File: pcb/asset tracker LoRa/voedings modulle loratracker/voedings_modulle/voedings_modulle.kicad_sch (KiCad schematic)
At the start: 3 parts

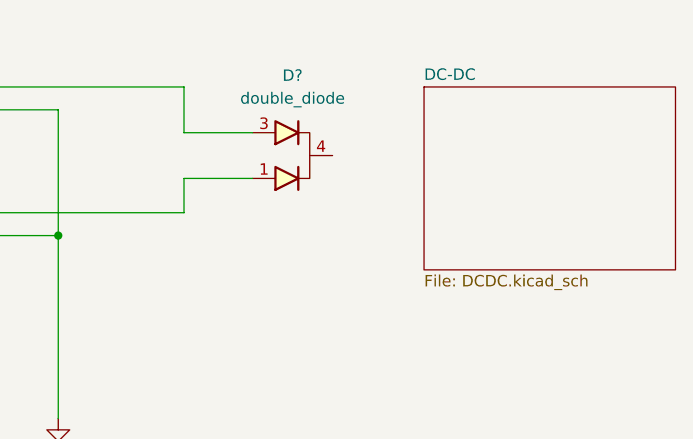
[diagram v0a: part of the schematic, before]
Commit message: ref design
esp32prog refrence design
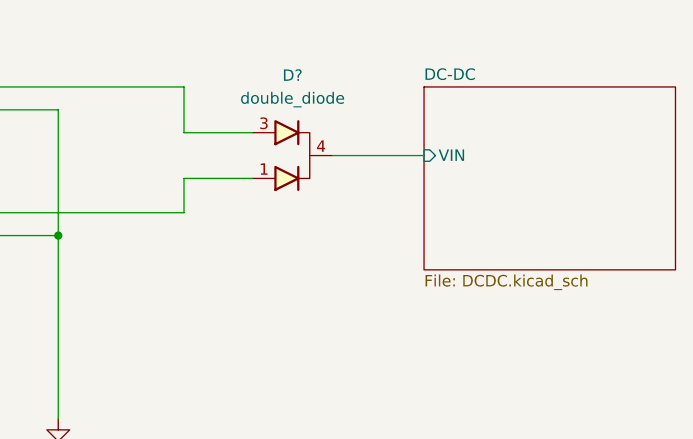
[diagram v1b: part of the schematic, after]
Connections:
- net DC-DC/VIN: now reaches D?.2, D?.4
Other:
- sheet DC-DC ports: added VIN; removed none
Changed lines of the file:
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@@
+    (stroke (width 0) (type solid) (color 0 0 0 0))
+  )
+  (wire (pts (xy 74.93 72.39) (xy 85.09 72.39))
     (stroke (width 0) (type solid) (color 0 0 0 0))
   )
@@
       (effects (font (size 1.27 1.27)) (justify left top))
     )
+    (pin "VIN" input (at 85.09 72.39 180)
+      (effects (font (size 1.27 1.27)) (justify left))
+    )
   )

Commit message: wef
wef
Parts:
- D1: renamed from D?; value double_diode -> MBR1560CT; footprint (none) -> halfgeleiders:DPAK
- con1: renamed from con?; value battery_con -> screw terminal
- con2: renamed from con?; value battery_con -> xt60
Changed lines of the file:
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@@
   (symbol (lib_id "power:GND") (at 44.45 101.6 0) (unit 1)
     (in_bom yes) (on_board yes) (fields_autoplaced)
-    (property "Reference" "#PWR?" (id 0) (at 44.45 107.95 0)
+    (property "Reference" "#PWR0101" (id 0) (at 44.45 107.95 0)
       (effects (font (size 1.27 1.27)) hide)
     )
@@
   (symbol (lib_id "conectors:battery_con") (at 27.94 66.04 0) (mirror y) (unit 1)
     (in_bom yes) (on_board yes) (fields_autoplaced)
-    (property "Reference" "con?" (id 0) (at 28.7655 58.42 0))
-    (property "Value" "battery_con" (id 1) (at 28.7655 60.96 0))
+    (property "Reference" "con1" (id 0) (at 28.7655 58.42 0))
+    (property "Value" "screw terminal" (id 1) (at 28.7655 60.96 0))
     (property "Footprint" "" (id 2) (at 27.94 66.04 0)
       (effects (font (size 1.27 1.27)) hide)
@@
   (symbol (lib_id "conectors:battery_con") (at 27.94 80.01 0) (mirror y) (unit 1)
     (in_bom yes) (on_board yes) (fields_autoplaced)
-    (property "Reference" "con?" (id 0) (at 28.7655 72.39 0))
-    (property "Value" "battery_con" (id 1) (at 28.7655 74.93 0))
+    (property "Reference" "con2" (id 0) (at 28.7655 72.39 0))
+    (property "Value" "xt60" (id 1) (at 28.7655 74.93 0))
     (property "Footprint" "" (id 2) (at 27.94 80.01 0)
       (effects (font (size 1.27 1.27)) hide)
@@
   (symbol (lib_id "Halfgelijders:double_diode") (at 72.39 72.39 270) (unit 1)
     (in_bom yes) (on_board yes) (fields_autoplaced)
-    (property "Reference" "D?" (id 0) (at 70.485 63.5 90))
-    (property "Value" "double_diode" (id 1) (at 70.485 66.04 90))
-    (property "Footprint" "" (id 2) (at 74.93 72.39 0)
+    (property "Reference" "D1" (id 0) (at 70.485 63.5 90))
+    (property "Value" " MBR1560CT" (id 1) (at 70.485 66.04 90))
+    (property "Footprint" "halfgeleiders:DPAK" (id 2) (at 74.93 72.39 0)
       (effects (font (size 1.27 1.27)) hide)
     )
@@
     (pin "4")
   )
-  (sheet (at 85.09 64.77) (size 27.94 20.32) (fields_autoplaced)
+  (sheet (at 85.09 69.85) (size 12.7 6.35) (fields_autoplaced)
     (stroke (width 0.0006) (type solid) (color 0 0 0 0))
     (fill (color 0 0 0 0.0000))
-    (property "Sheet name" "DC-DC" (id 0) (at 85.09 64.1343 0)
+    (property "Sheet name" "DC-DC" (id 0) (at 85.09 69.2143 0)
       (effects (font (size 1.27 1.27)) (justify left bottom))
     )
-    (property "Sheet file" "DCDC.kicad_sch" (id 1) (at 85.09 85.5987 0)
+    (property "Sheet file" "DCDC.kicad_sch" (id 1) (at 85.09 76.7087 0)
       (effects (font (size 1.27 1.27)) (justify left top))
     )
@@
   (symbol_instances
     (path "/b69da6a5-0c3e-4852-84f1-f7d176af5178"
-      (reference "#PWR?") (unit 1) (value "GND") (footprint "")
+      (reference "#PWR0101") (unit 1) (value "GND") (footprint "")
+    )
+    (path "/6da2fc13-0bf2-46cb-b2dd-779a7fa447fa/2973d96f-90c0-4ae4-8021-b72c068276ee"
+      (reference "#PWR0102") (unit 1) (value "GND") (footprint "")
+    )
+    (path "/6da2fc13-0bf2-46cb-b2dd-779a7fa447fa/21b9ad56-b1d7-46eb-b3cc-830247fa8880"
+      (reference "#PWR0103") (unit 1) (value "GND") (footprint "")
+    )
+    (path "/6da2fc13-0bf2-46cb-b2dd-779a7fa447fa/dc1cd67e-94ec-429f-aefd-baf227c16e17"
+      (reference "#PWR0104") (unit 1) (value "GND") (footprint "")
+    )
+    (path "/6da2fc13-0bf2-46cb-b2dd-779a7fa447fa/176d8147-3e32-469d-8144-7c1e37eee731"
+      (reference "#PWR0105") (unit 1) (value "GND") (footprint "")
+    )
+    (path "/6da2fc13-0bf2-46cb-b2dd-779a7fa447fa/283da580-96bb-41c1-b1bc-b132a72a227e"
+      (reference "#PWR0106") (unit 1) (value "GND") (footprint "")
+    )
+    (path "/6da2fc13-0bf2-46cb-b2dd-779a7fa447fa/a635c1e6-72a8-4ee4-bf7c-4edf8782d9ad"
+      (reference "#PWR0107") (unit 1) (value "GND") (footprint "")
+    )
+    (path "/6da2fc13-0bf2-46cb-b2dd-779a7fa447fa/5b99cbd5-d1ec-4d26-a902-cdaf328a07cd"
+      (reference "C1") (unit 1) (value "C_Small") (footprint "")
+    )
+    (path "/6da2fc13-0bf2-46cb-b2dd-779a7fa447fa/fd0ed657-0818-4d37-bda3-c4b52abdd616"
+      (reference "C2") (unit 1) (value "C_Small") (footprint "")
+    )
+    (path "/6da2fc13-0bf2-46cb-b2dd-779a7fa447fa/6cc34a28-62b2-4820-ad9f-ca8cc24addbb"
+      (reference "C3") (unit 1) (value "C") (footprint "")
+    )
+    (path "/6da2fc13-0bf2-46cb-b2dd-779a7fa447fa/4f48aa7e-168d-49da-a8c3-54ed476f0384"
+      (reference "C4") (unit 1) (value "C_Polarized_Small_US") (footprint "")
     )
     (path "/f814b072-693b-4a39-959d-cba41b429442"
-      (reference "D?") (unit 1) (value "double_diode") (footprint "")
+      (reference "D1") (unit 1) (value " MBR1560CT") (footprint "halfgeleiders:DPAK")
+    )
+    (path "/6da2fc13-0bf2-46cb-b2dd-779a7fa447fa/735a1f33-a5df-4021-b2a8-372e5f7e6f84"
+      (reference "D2") (unit 1) (value "D_Schottky") (footprint "")
+    )
+    (path "/6da2fc13-0bf2-46cb-b2dd-779a7fa447fa/af55fb99-7bae-4961-bd23-b38d7025c33a"
+      (reference "J1") (unit 1) (value "Screw_Terminal_01x02") (footprint "")
+    )
+    (path "/6da2fc13-0bf2-46cb-b2dd-779a7fa447fa/463799d9-45f8-4963-af3f-d0632981f49c"
+      (reference "L1") (unit 1) (value "L") (footprint "")
+    )
+    (path "/6da2fc13-0bf2-46cb-b2dd-779a7fa447fa/35ef0e3a-24f6-45fa-83f5-f2c157a8910b"
+      (reference "R1") (unit 1) (value "R_Small_US") (footprint "")
+    )
+    (path "/6da2fc13-0bf2-46cb-b2dd-779a7fa447fa/c94f7291-0b6b-43a7-ba37-196443e92db9"
+      (reference "R2") (unit 1) (value "R_Small_US") (footprint "")
+    )
+    (path "/6da2fc13-0bf2-46cb-b2dd-779a7fa447fa/5e9287ae-c1ac-44c7-b8fe-5697a4e9971c"
+      (reference "U1") (unit 1) (value "MAX5035AUSA") (footprint "Package_SO:SOIC-8_3.9x4.9mm_P1.27mm")
+    )
+    (path "/a5a6b075-b381-4de0-8cb2-1f154fbb764c"
+      (reference "con1") (unit 1) (value "screw terminal") (footprint "")
     )
     (path "/5ae77b84-2a40-4e44-92ae-4561547d1029"
-      (reference "con?") (unit 1) (value "battery_con") (footprint "")
-    )
-    (path "/a5a6b075-b381-4de0-8cb2-1f154fbb764c"
-      (reference "con?") (unit 1) (value "battery_con") (footprint "")
+      (reference "con2") (unit 1) (value "xt60") (footprint "")
     )
   )

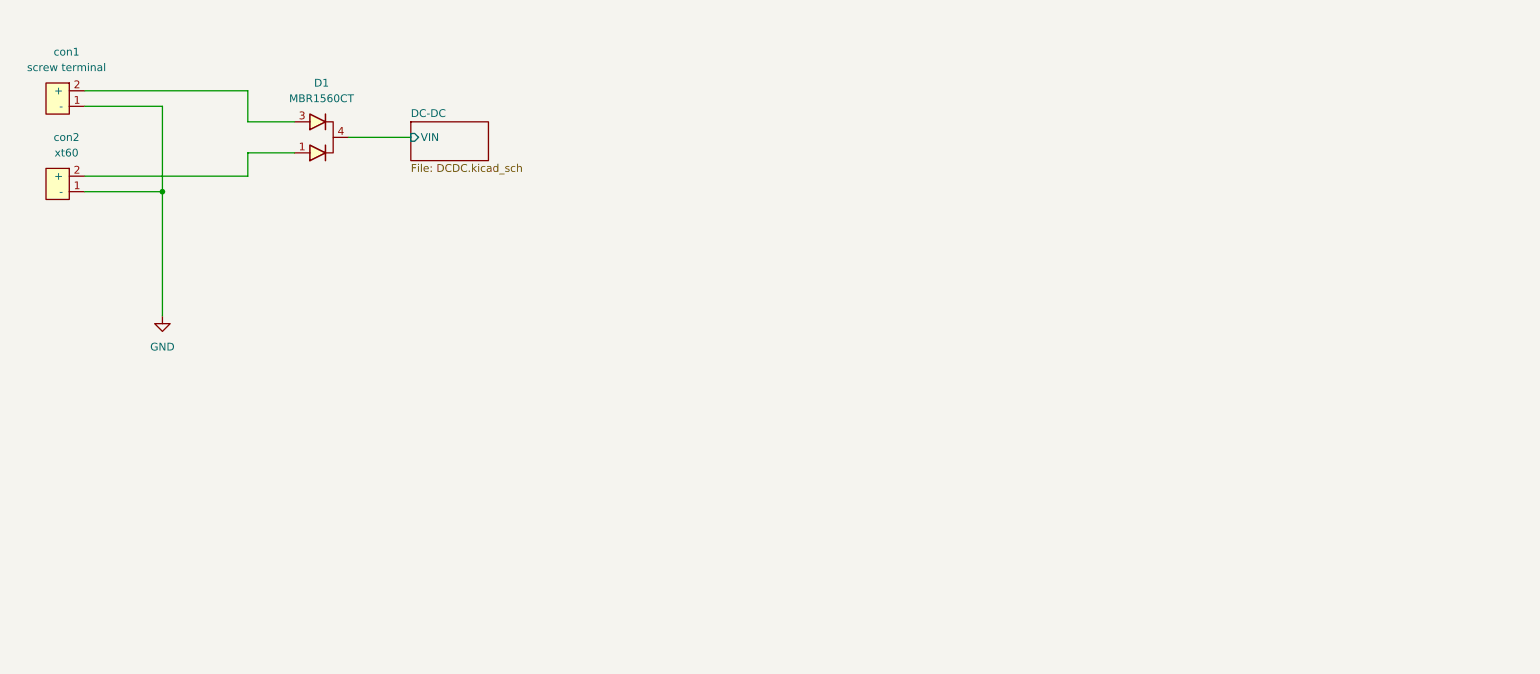
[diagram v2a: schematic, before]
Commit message: voedings PCB
Voedings pcb schema afgetekend
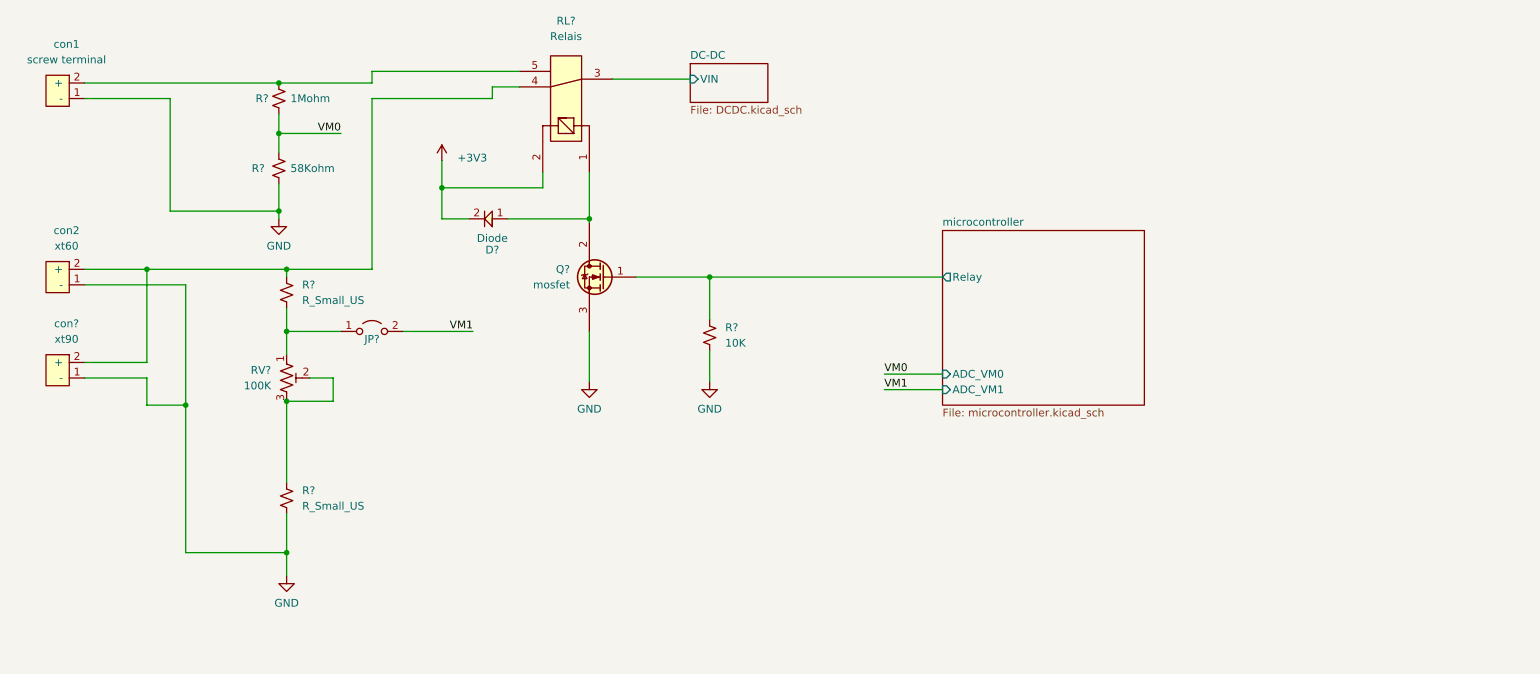
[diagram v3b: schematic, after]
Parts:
- removed D1: MBR1560CT, halfgeleiders:DPAK, symbol Halfgelijders:double_diode
- added D?: Diode, symbol Halfgelijders:Diode
- added JP?: Jumper_2_Open, symbol Jumper:Jumper_2_Open
- added Q?: mosfet, symbol Halfgelijders:mosfet
- added R?: 10K, symbol Device:R_Small_US
- added R?: 58Kohm, symbol Device:R_Small_US
- added R? (x2): R_Small_US, symbol Device:R_Small_US
- added R?: 1Mohm, symbol Device:R_Small_US
- added RL?: Relais, symbol vanalles:Relais
- added RV?: 100K, symbol Device:R_Potentiometer_Trim_US
- added con?: xt90, symbol conectors:battery_con
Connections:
- net DC-DC/VIN: now also RL?.3
- net GND: now also Q?.3, R?.2, R?.2, R?.2, con?.1 (-)
- net at con2.2 (+): now also R?.1, RL?.4, con?.2 (+)
- net at con1.2 (+): now also R?.1, RL?.5
- new net: D?.1, Q?.2, RL?.1
- new net: JP?.1 (A), R?.2, RV?.1
- new net: R?.1, RV?.2, RV?.3
- new net +3V3: D?.2, RL?.2
- new net VM0: R?.1, R?.2
- new net VM1: JP?.2 (B)
- new net microcontroller/Relay: Q?.1, R?.1
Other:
- added sheet microcontroller (microcontroller.kicad_sch)
- moved on the sheet: con1, con2

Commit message: schema voedingswitcher af
voeding switcher voor v1 afgetekend
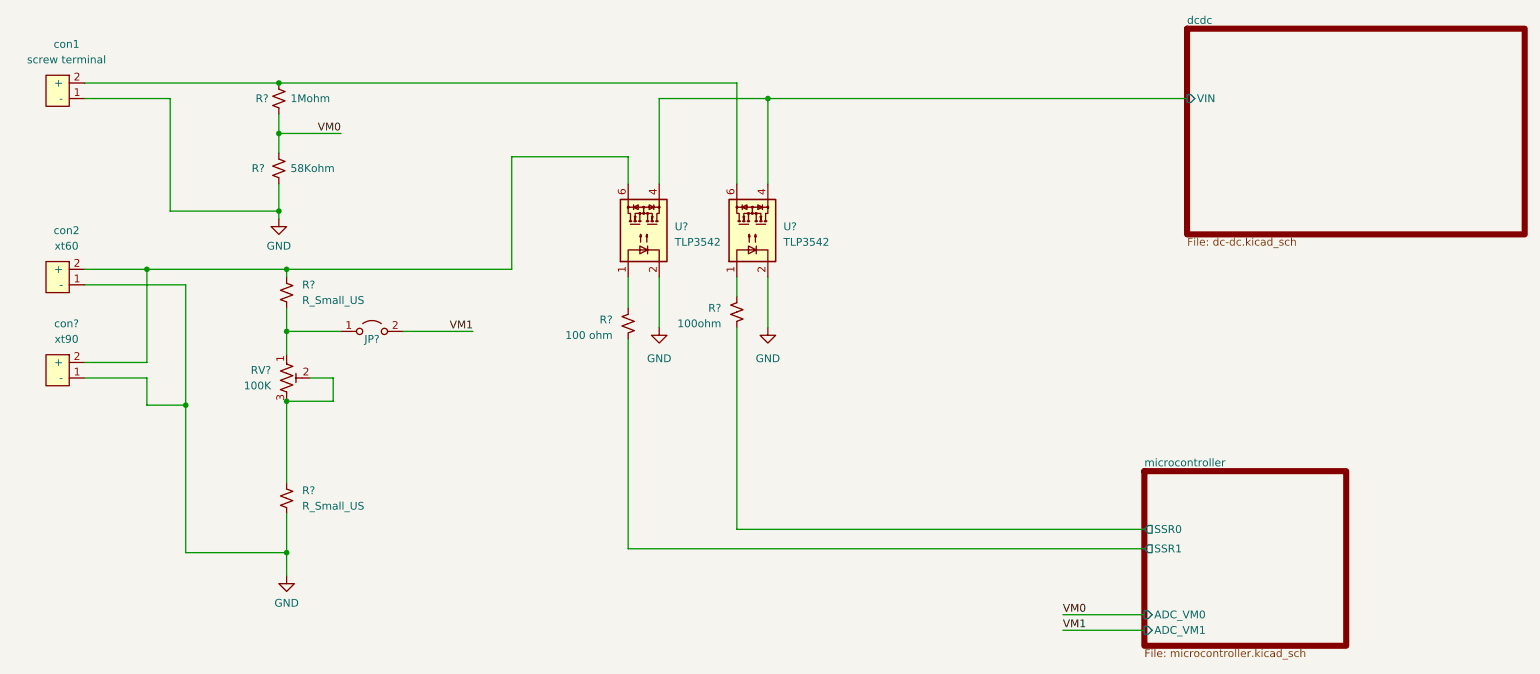
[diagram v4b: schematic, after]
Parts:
- removed D?: Diode, symbol Halfgelijders:Diode
- removed Q?: mosfet, symbol Halfgelijders:mosfet
- removed R?: 10K, symbol Device:R_Small_US
- removed RL?: Relais, symbol vanalles:Relais
- added R?: 100ohm, symbol Device:R_Small_US
- added R?: 100 ohm, symbol Device:R_Small_US
- added U? (x2): TLP3542, Package_DIP:DIP-5-6_W7.62mm, symbol Relay_SolidState:TLP3542
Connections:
- net GND: now also U?.2, U?.2
- net at R?.1, con2.2 (+), con?.2 (+): now also U?.6
- net at R?.1, con1.2 (+): now also U?.6
- new net: R?.2, U?.1 (x2)
- new net dcdc/VIN: U?.4, U?.4
- new net microcontroller/SSR0: R?.1
- new net microcontroller/SSR1: R?.1
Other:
- removed sheet DC-DC
- added sheet dcdc (dc-dc.kicad_sch)
- sheet microcontroller ports: added SSR0, SSR1; removed Relay
